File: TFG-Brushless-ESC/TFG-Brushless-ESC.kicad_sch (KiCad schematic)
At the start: 57 parts, among them J1 24V IN, J2 MOTOR, J5 USB C Receptacle, J6 HALL SENSORS, J7 SWD, SW1 BOOT0, SW2 NRST, U1 LM317, U2 LM317, U3 STM32F411CEUx, Y1 25MHz, Y2 32.768kHz

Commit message: temporary unifinished layout
tht components and initia layout
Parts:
- removed C43: 2u2, Capacitor_THT:CP_Radial_D5.0mm_P2.00mm, symbol Device:C_Polarized_US
- removed U1: LM317, Package_TO_SOT_THT:TO-220-3_Vertical, symbol Regulator_Linear:LM317_TO-220
- added C24: 10u, Capacitor_THT:CP_Radial_D5.0mm_P2.00mm, symbol Device:C_Polarized_US
- added D8: D5V0L2B3T, Package_TO_SOT_SMD:SOT-523, symbol TFG-Brushless-ESC:Dual-TVS
- added J3: I2C, Connector_PinHeader_2.54mm:PinHeader_1x04_P2.54mm_Vertical, symbol Connector_Generic:Conn_01x04
- added U10: LM317L_SOT-89, Package_TO_SOT_SMD:SOT-89-3, symbol Regulator_Linear:LM317L_SOT-89
- D15: value SMAJ16CA-13-F -> DESD5V0U1BA; footprint Diode_SMD:D_SMA -> Diode_SMD:D_SOD-323_HandSoldering
- F1: footprint (none) -> TFG-Brushless-ESC:Fuseholder_Automotive
- F2: footprint (none) -> Fuse:Fuse_1812_4532Metric
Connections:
- net +12V: now also R2.1, U2.2 (VO); no longer R4.2, R7.2, U2.1 (ADJ)
- net +24V: now also C24.1
- net +3V3: now also J6.5 (Pin_5), J3.1 (Pin_1), U10.2 (VO); no longer J6.1 (Pin_1)
- net +5V: now also U10.3 (VI)
- net BOOT0: now also C13.2, R8.2, SW2.2 (B), U3.44 (BOOT0); no longer C7.2, R5.2, SW1.2 (B), U3.7 (NRST)
- net GND: now also J1.1 (Pin_1), J6.1 (Pin_1), C24.2, D8.3, J3.4 (Pin_4); no longer J1.2 (Pin_2), J6.5 (Pin_5)
- net NRST: now also C7.2, R5.2, SW1.2 (B), U3.7 (NRST); no longer C13.2, R8.2, SW2.2 (B), U3.44 (BOOT0)
- net PA10: now also J6.2 (Pin_2), R36.1
- net PA15: now also D2.1 (K)
- net PA8: now also J6.4 (Pin_4), R34.1
- net PA9: now also J6.3 (Pin_3), R35.1
- net PB1: no longer J6.2 (Pin_2), R34.1
- net PB10: no longer J6.4 (Pin_4), R36.1
- net PB2: no longer J6.3 (Pin_3), R35.1
- net PC13: no longer D2.1 (K)
- net USB_R_N: now also D8.1
- net USB_R_P: now also D8.2
- net V_DIV_3: now also U10.1 (ADJ)
- net 24V in: now reaches F1.1
- net 24V in: now also J1.2 (Pin_2); no longer J1.1 (Pin_1)
- net 24V fused: now reaches D13.1 (A), D13.3 (A), D14.2 (A2), F1.2
- net 5V fused: now reaches D12.2 (A), D15.2 (A2), F2.2
- net PB8 renamed I2C_SCL
- net I2C_SCL: now also J3.3 (Pin_3)
- net PB9 renamed I2C_SDA
- net I2C_SDA: now also J3.2 (Pin_2)
- new net V_DIV_12: R4.2, R7.2, U2.1 (ADJ)
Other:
- note added: "Connector protection"
- moved on the sheet: C11, C18, D12, D13, D14, D15, F1, F2, J1, J2, J5, J6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

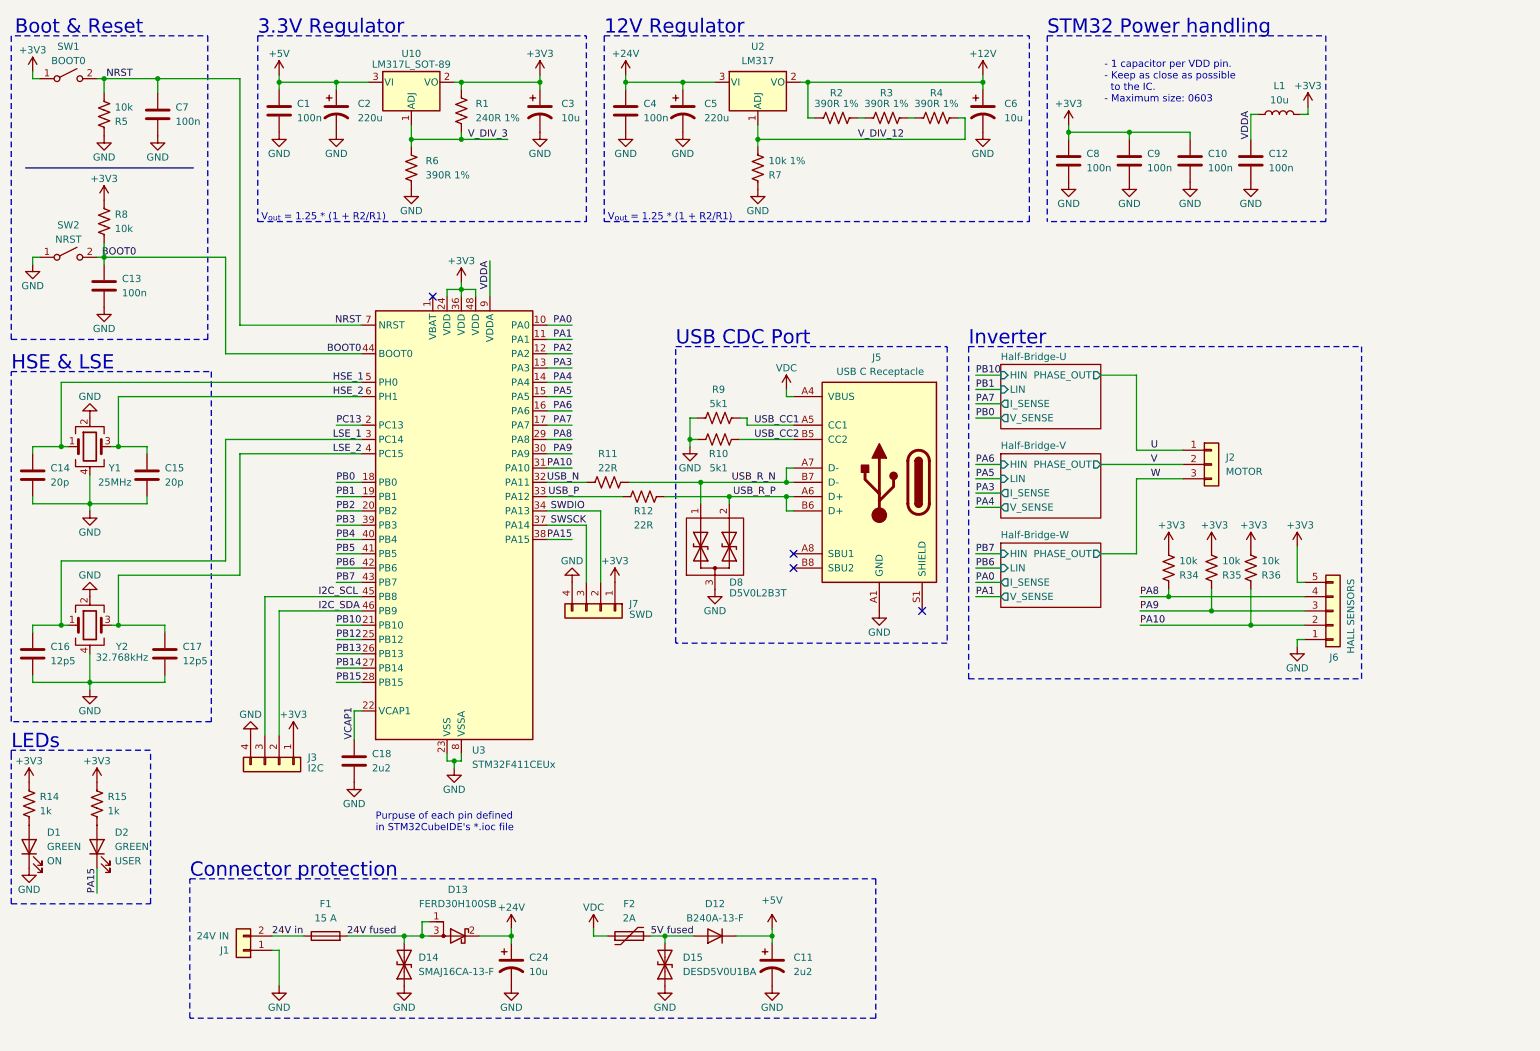
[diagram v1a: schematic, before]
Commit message: updated code to match pinout
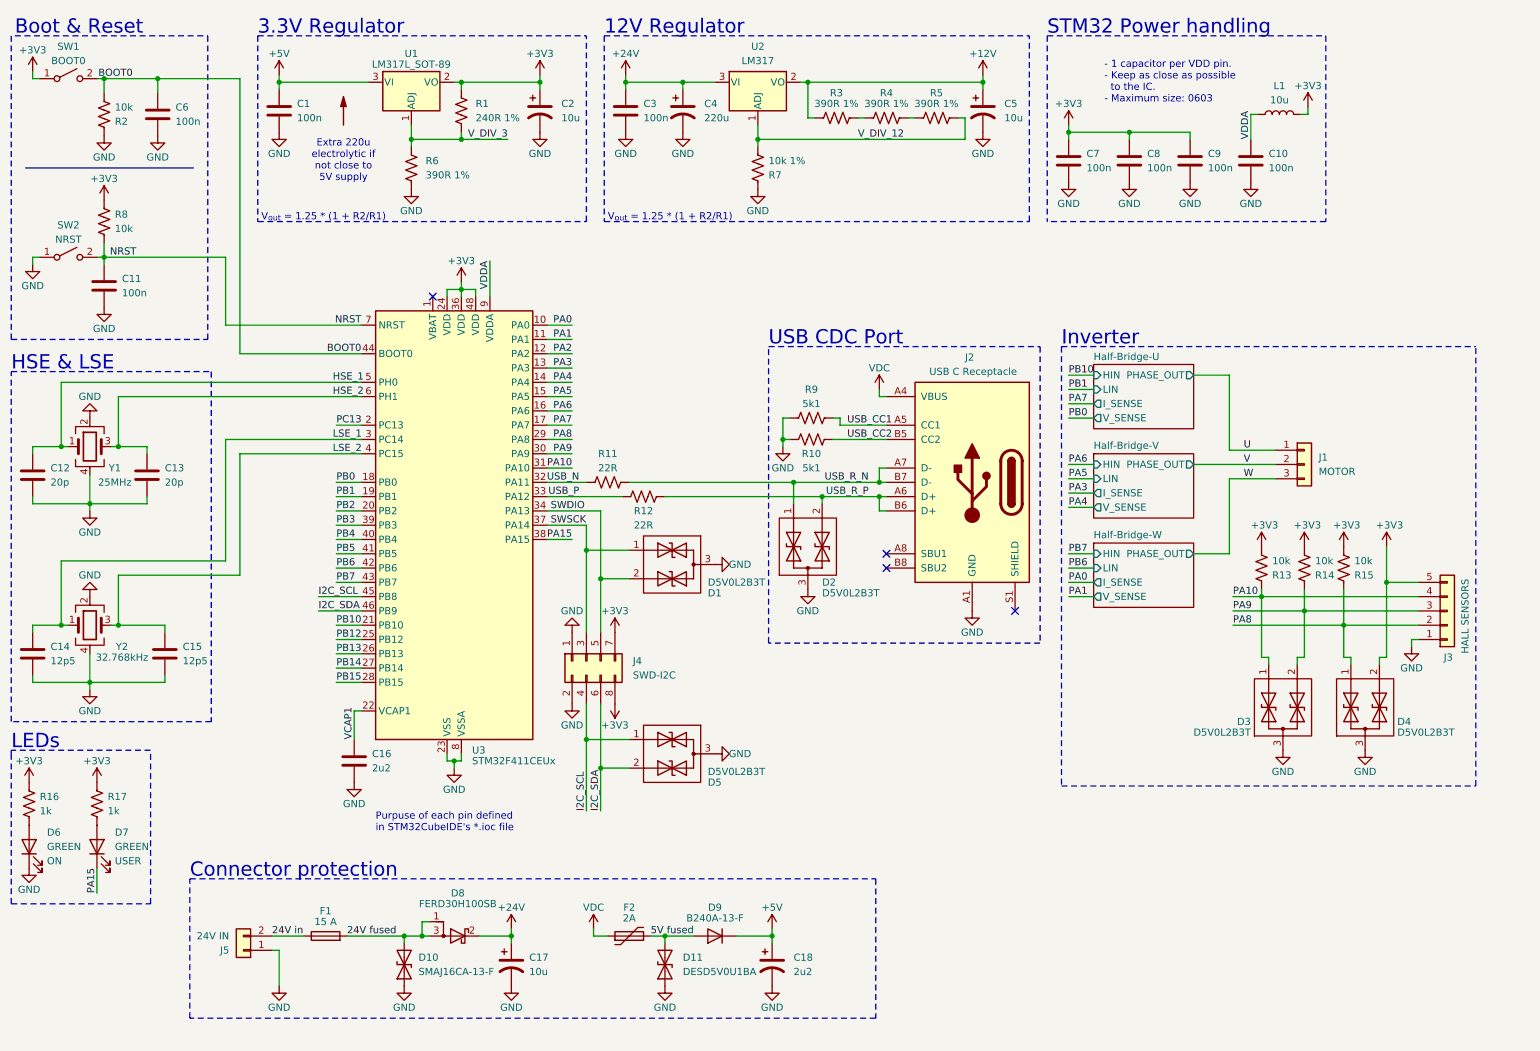
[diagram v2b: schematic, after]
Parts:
- removed C2: 220u, Capacitor_THT:CP_Radial_D5.0mm_P2.00mm, symbol Device:C_Polarized_US
- removed J3: I2C, Connector_PinHeader_2.54mm:PinHeader_1x04_P2.54mm_Vertical, symbol Connector_Generic:Conn_01x04
- removed J7: SWD, Connector_PinHeader_2.54mm:PinHeader_1x04_P2.54mm_Vertical, symbol Connector_Generic:Conn_01x04
- added D1, D3, D4, D5: D5V0L2B3T, Package_TO_SOT_SMD:SOT-523, symbol TFG-Brushless-ESC:Dual-TVS
- added J4: SWD-I2C, Connector_PinHeader_2.54mm:PinHeader_2x04_P2.54mm_Horizontal, symbol Connector_Generic:Conn_02x04_Odd_Even
- C17: renamed from C24; footprint Capacitor_THT:CP_Radial_D5.0mm_P2.00mm -> Capacitor_SMD:CP_Elec_4x5.4
- C18: renamed from C11; footprint Capacitor_THT:CP_Radial_D5.0mm_P2.00mm -> Capacitor_SMD:CP_Elec_4x5.4
- C2: renamed from C3; footprint Capacitor_THT:CP_Radial_D5.0mm_P2.00mm -> Capacitor_SMD:CP_Elec_4x5.4
- C4: renamed from C5; footprint Capacitor_THT:CP_Radial_D5.0mm_P2.00mm -> Capacitor_SMD:CP_Elec_4x5.4
- C5: renamed from C6; footprint Capacitor_THT:CP_Radial_D5.0mm_P2.00mm -> Capacitor_SMD:CP_Elec_4x5.4
- J3: renamed from J6; footprint Connector_JST:JST_PH_B5B-PH-SM4-TB_1x05-1MP_P2.00mm_Vertical -> Connector_JST:JST_PH_S5B-PH-K_1x05_P2.00mm_Horizontal
- renumbered C12 to C10, C13 to C11, C14 to C12, C15 to C13, C16 to C14, C17 to C15, C18 to C16, C4 to C3, C7 to C6, C8 to C7, C9 to C8, C10 to C9, D14 to D10, D15 to D11, D8 to D2, D1 to D6, D2 to D7, D13 to D8, D12 to D9, J2 to J1, J5 to J2, J1 to J5, R34 to R13, R35 to R14, R36 to R15, R14 to R16, R15 to R17, R5 to R2, R2 to R3, R3 to R4, R4 to R5, U10 to U1
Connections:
- net +3V3: now also D4.2, J4.7 (Pin_7), J4.8 (Pin_8)
- net BOOT0: now also C6.2, R2.2, SW1.2 (B); no longer C11.2, R8.2, SW2.2 (B)
- net GND: now also D1.3, D3.3, D4.3, D5.3, J4.1 (Pin_1), J4.2 (Pin_2)
- net I2C_SCL: now also D5.1, J4.4 (Pin_4)
- net I2C_SDA: now also D5.2, J4.6 (Pin_6)
- net NRST: now also C11.2, R8.2, SW2.2 (B); no longer C6.2, R2.2, SW1.2 (B)
- net PA10: now also J3.4 (Pin_4), R13.1, D3.1; no longer J3.2 (Pin_2), R15.1
- net PA8: now also J3.2 (Pin_2), R15.1, D4.1; no longer J3.4 (Pin_4), R13.1
- net PA9: now also D3.2
- net SWDIO: now also D1.2, J4.5 (Pin_5)
- net SWSCK: now also D1.1, J4.3 (Pin_3)
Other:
- note added: "Extra 220u electrolytic if not close to 5V supply"
- moved on the sheet: D2, J1, J2, J3, R10, R13, R14, R15, R9

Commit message: Added pulldown resistors at motor output
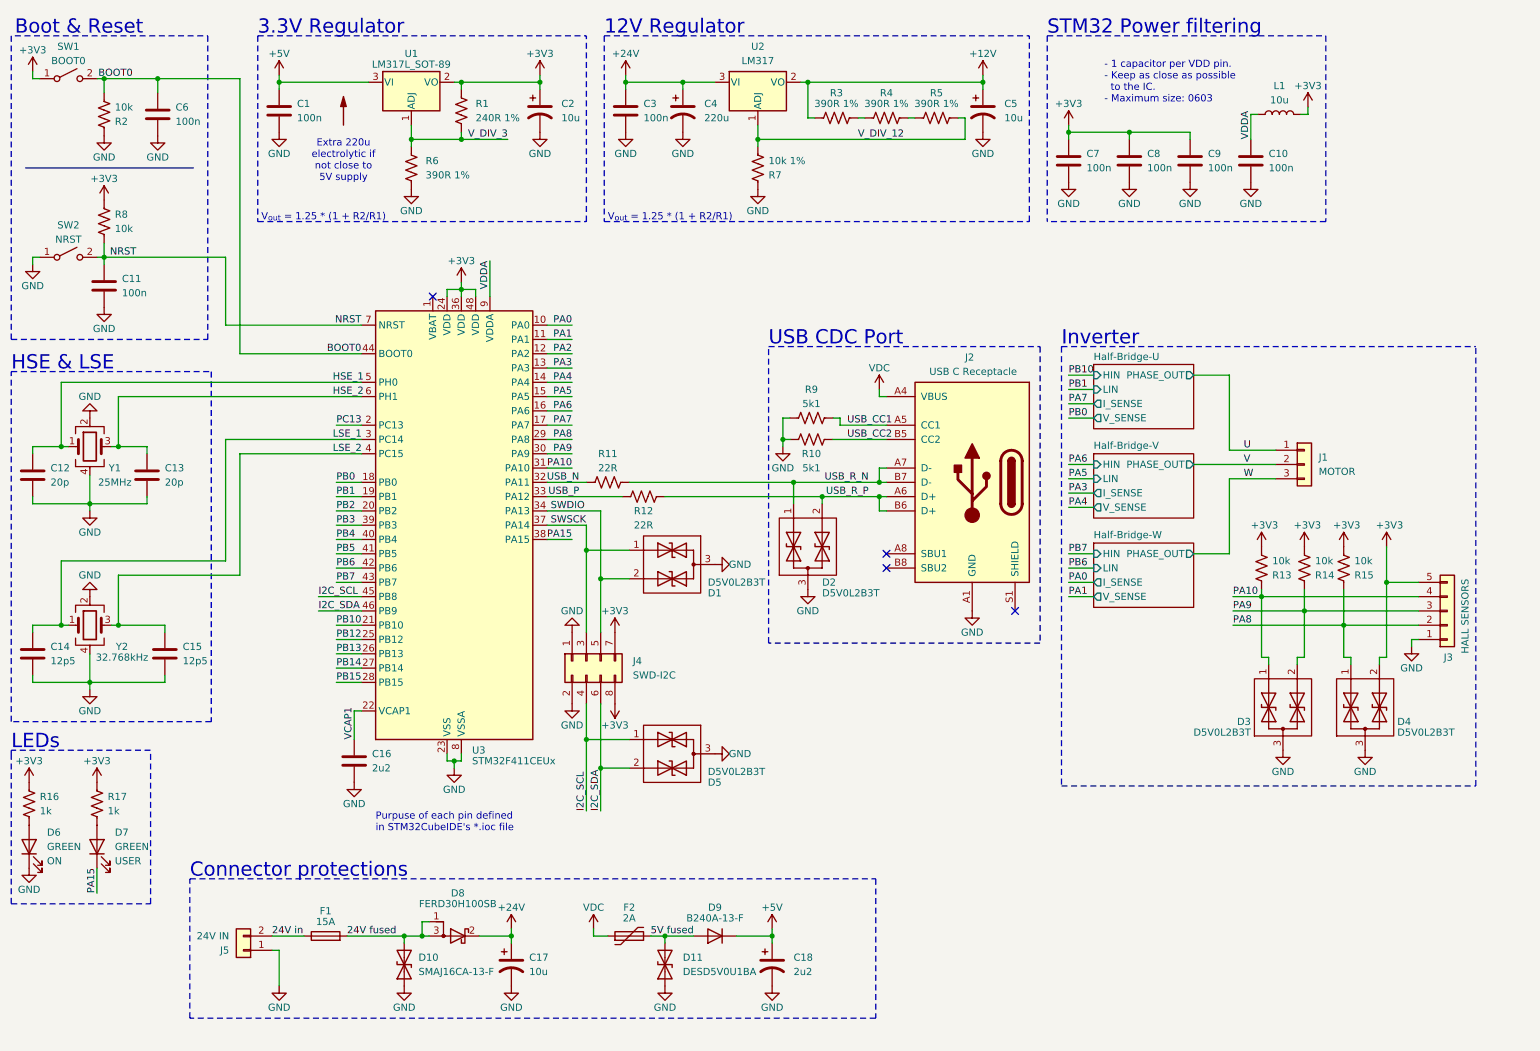
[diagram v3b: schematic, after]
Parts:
- F1: value 15 A -> 15A
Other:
- note added: "Connector protections"
- note added: "STM32 Power filtering"
- note removed: "Connector protection"
- note removed: "STM32 Power handling"
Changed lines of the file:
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@@
 		)
 	)
-	(text "STM32 Power handling"
+	(text "STM32 Power filtering"
 		(exclude_from_sim no)
 		(at 199.39 17.78 0)
@@
 		)
 	)
-	(text "Connector protection"
+	(text "Connector protections"
 		(exclude_from_sim no)
 		(at 46.99 167.64 0)
@@
 			)
 		)
-		(property "Value" "15 A"
+		(property "Value" "15A"
 			(at 71.12 175.26 90)
 			(effects
@@
 			)
 		)
-		(property "Datasheet" "~"
+		(property "Datasheet" "https://www.littelfuse.com/assetdocs/fuse-218-datasheet?assetguid=a96d72b7-5296-4815-88b4-98b2f6738874"
 			(at 71.12 177.8 0)
 			(effects
@@
 			)
 		)
-		(property "Datasheet" "~"
+		(property "Datasheet" "https://www.littelfuse.com/assetdocs/littelfuse_ptc_minismdc_datasheet?assetguid=3ed735aa-64ed-43a6-bc20-610590bc99c6"
 			(at 125.095 177.8 0)
 			(effects

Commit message: Slight code changes
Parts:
- added R42, R43, R44: 10k, Resistor_SMD:R_0603_1608Metric, symbol Device:R_US
- F1: value 15A -> 20A
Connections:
- net GND: now also R42.1, R43.1, R44.1
- net U: now also R42.2
- net V: now also R43.2
- net W: now also R44.2
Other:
- moved on the sheet: D3, D4, J1, J3, R13, R14, R15

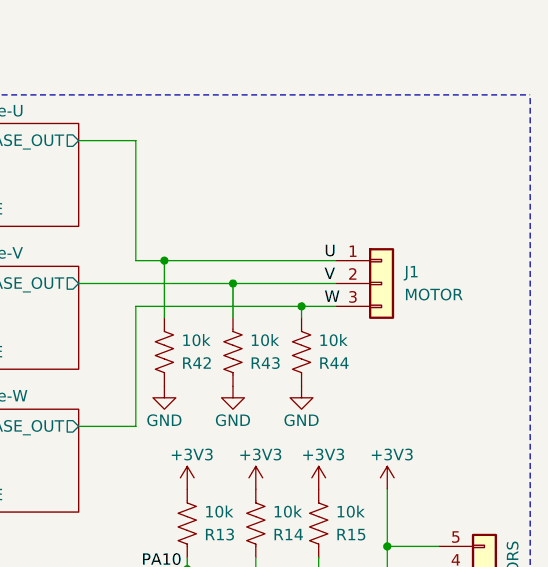
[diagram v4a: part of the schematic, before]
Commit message: Change motor terminal blocks and new half bridge layaout
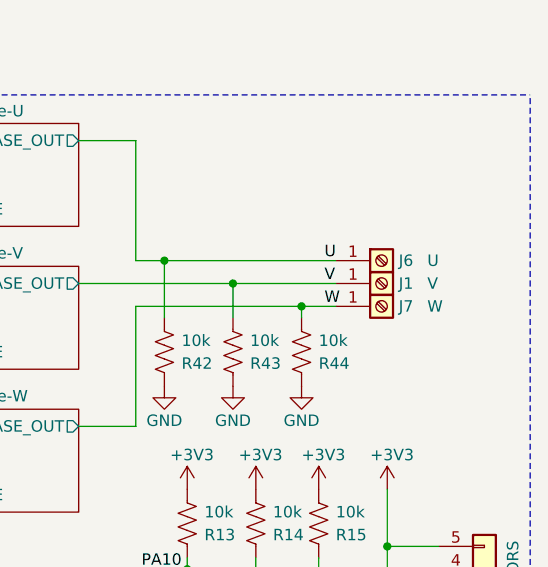
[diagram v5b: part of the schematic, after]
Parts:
- removed J1: MOTOR, TerminalBlock_Phoenix:TerminalBlock_Phoenix_MKDS-1,5-3-5.08_1x03_P5.08mm_Horizontal, symbol Connector_Generic:Conn_01x03
- added J1: V, TFG-Brushless-ESC:Screw_Terminal, symbol Connector:Screw_Terminal_01x01
- added J6: U, TFG-Brushless-ESC:Screw_Terminal, symbol Connector:Screw_Terminal_01x01
- added J7: W, TFG-Brushless-ESC:Screw_Terminal, symbol Connector:Screw_Terminal_01x01
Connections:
- net U: now also J6.1 (Pin_1)
- net V: now also J1.1 (Pin_1)
- net W: now also J7.1 (Pin_1)

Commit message: PCB v2
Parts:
- added D24, D25: DESD5V0U1BA, Diode_SMD:D_SOD-323_HandSoldering, symbol Device:D_TVS
- added R45, R46: 10k, Resistor_SMD:R_0603_1608Metric, symbol Device:R_US
- F1: value 20A -> 15A; Holder datasheet (none) -> https://www.lcsc.com/datasheet/lcsc_datasheet_2410121830_XF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
- J2: footprint Connector_USB:USB_C_Receptacle_G-Switch_GT-USB-7010ASV -> Connector_USB:USB_C_Receptacle_XKB_U262-16XN-4BVC11
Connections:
- net +12V: now also D25.2 (A2)
- net +3V3: now also D24.2 (A2), R45.2, R46.2
- net GND: now also D24.1 (A1), D25.1 (A1)
- net I2C_SCL: now also R45.1
- net I2C_SDA: now also R46.1
- net PA10: now also D4.1, R15.1; no longer D3.1, R13.1
- net PA8: now also D3.1, R13.1; no longer D4.1, R15.1
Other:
- moved on the sheet: C10, C17, C18, C3, C4, C5, C7, C8, C9, D10, D11, D5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
